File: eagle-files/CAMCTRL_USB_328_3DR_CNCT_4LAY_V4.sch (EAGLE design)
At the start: 71 parts, among them IC2 lm1117, J1 ICSP, Q1 12MHz, U1 M3421E, U2 ATMEGA168, U3 3.3V_REG, U4 TS3USB30EDGSR, Y1 16MHz

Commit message: Updated Code and Board
Updated test code with new object info handling, zooming command and
some extra clean-ups.
Board updated with replaced LED's resistors.
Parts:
- R13, R2, R6: value 1K -> 220R
- R14: value 330 -> 100R
- R17, R18: value 270R -> 220R
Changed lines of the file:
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@@
 <part name="Y1" library="SparkFun-FreqCtrl" deviceset="RESONATOR" device="16MHZ" value="16MHz"/>
 <part name="Q1" library="SparkFun-FreqCtrl" deviceset="CRYSTAL" device="5X3" value="12MHz"/>
-<part name="R2" library="pel_dipol_comp" deviceset="RESISTOR" device="-0402" value="1K"/>
+<part name="R2" library="pel_dipol_comp" deviceset="RESISTOR" device="-0402" value="220R"/>
 <part name="C2" library="pel_dipol_comp" deviceset="CAPACITOR" device="-0402" value="0.1uF"/>
 <part name="P+1" library="supply1" deviceset="VCC" device="" value="5V"/>
@@
 <part name="LED2" library="pel_dipol_comp" deviceset="LED" device="-0603" value="RED"/>
 <part name="GND16" library="SparkFun" deviceset="GND" device=""/>
-<part name="R14" library="pel_dipol_comp" deviceset="RESISTOR" device="-0402" value="330"/>
+<part name="R14" library="pel_dipol_comp" deviceset="RESISTOR" device="-0402" value="100R"/>
 <part name="C10" library="SparkFun" deviceset="CAP_POL" device="1206" value="10uF"/>
 <part name="GND17" library="SparkFun" deviceset="GND" device=""/>
@@
 <part name="R1" library="pel_dipol_comp" deviceset="RESISTOR" device="-0402" value="33 1%"/>
 <part name="R5" library="pel_dipol_comp" deviceset="RESISTOR" device="-0402" value="33 1%"/>
-<part name="R6" library="pel_dipol_comp" deviceset="RESISTOR" device="-0402" value="1K"/>
+<part name="R6" library="pel_dipol_comp" deviceset="RESISTOR" device="-0402" value="220R"/>
 <part name="GND18" library="supply1" deviceset="GND" device=""/>
 <part name="LED3" library="pel_dipol_comp" deviceset="LED" device="-0603" value="BLUE"/>
@@
 <part name="SJ1" library="SparkFun-Passives" deviceset="SOLDERJUMPER_2WAY" device="PASTE2&amp;3"/>
 <part name="SJ2" library="SparkFun-Passives" deviceset="SOLDERJUMPER-OLD" device="NO"/>
-<part name="R13" library="pel_dipol_comp" deviceset="RESISTOR" device="-0402" value="1K"/>
+<part name="R13" library="pel_dipol_comp" deviceset="RESISTOR" device="-0402" value="220R"/>
 <part name="LED4" library="pel_dipol_comp" deviceset="LED" device="-0603" value="BLUE"/>
 <part name="GND23" library="SparkFun-Aesthetics" deviceset="GND" device=""/>
@@
 <part name="C13" library="pel_dipol_comp" deviceset="CAPACITOR" device="-0402" value="0.1uF"/>
 <part name="GND30" library="SparkFun" deviceset="GND" device=""/>
-<part name="R17" library="pel_dipol_comp" deviceset="RESISTOR" device="-0402" value="270R"/>
-<part name="R18" library="pel_dipol_comp" deviceset="RESISTOR" device="-0402" value="270R"/>
+<part name="R17" library="pel_dipol_comp" deviceset="RESISTOR" device="-0402" value="220R"/>
+<part name="R18" library="pel_dipol_comp" deviceset="RESISTOR" device="-0402" value="220R"/>
 <part name="LED5" library="pel_dipol_comp" deviceset="LED" device="-0603" value="GREEN"/>
 <part name="LED6" library="pel_dipol_comp" deviceset="LED" device="-0603" value="RED"/>
@@
 <instance part="GND10" gate="1" x="45.72" y="185.42"/>
 <instance part="U$3" gate="G$1" x="45.72" y="220.98"/>
-<instance part="R4" gate="G$1" x="45.72" y="210.82" rot="R90"/>
+<instance part="R4" gate="G$1" x="45.72" y="210.82" smashed="yes" rot="R90">
+<attribute name="VALUE" x="48.768" y="210.82" size="1.778" layer="96" rot="R90"/>
+<attribute name="NAME" x="48.768" y="205.74" size="1.778" layer="95" rot="R90"/>
+</instance>
 <instance part="C14" gate="G$1" x="38.1" y="205.74" rot="R90"/>
 <instance part="C1" gate="G$1" x="96.52" y="391.16"/>

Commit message: Prototype V2
USB interruption line added;
VCC vs 5V wrong propagation corrected.
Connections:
- removed net D9: DIGITAL_PINS.2, U2.PB1(OC1A)
- removed net N$11: R3.2, U1.INT
- removed net VCC: C6.1, U4.VCC, U5.VCCB
- new net INT: R3.2, U1.INT, U2.PB1(OC1A)
- net 3.3V: now also U4.VCC
- net 5V: now also C6.1, U5.VCCB
- net D2: now also DIGITAL_PINS.2
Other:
- moved on the sheet: C3, C4, C5, C6

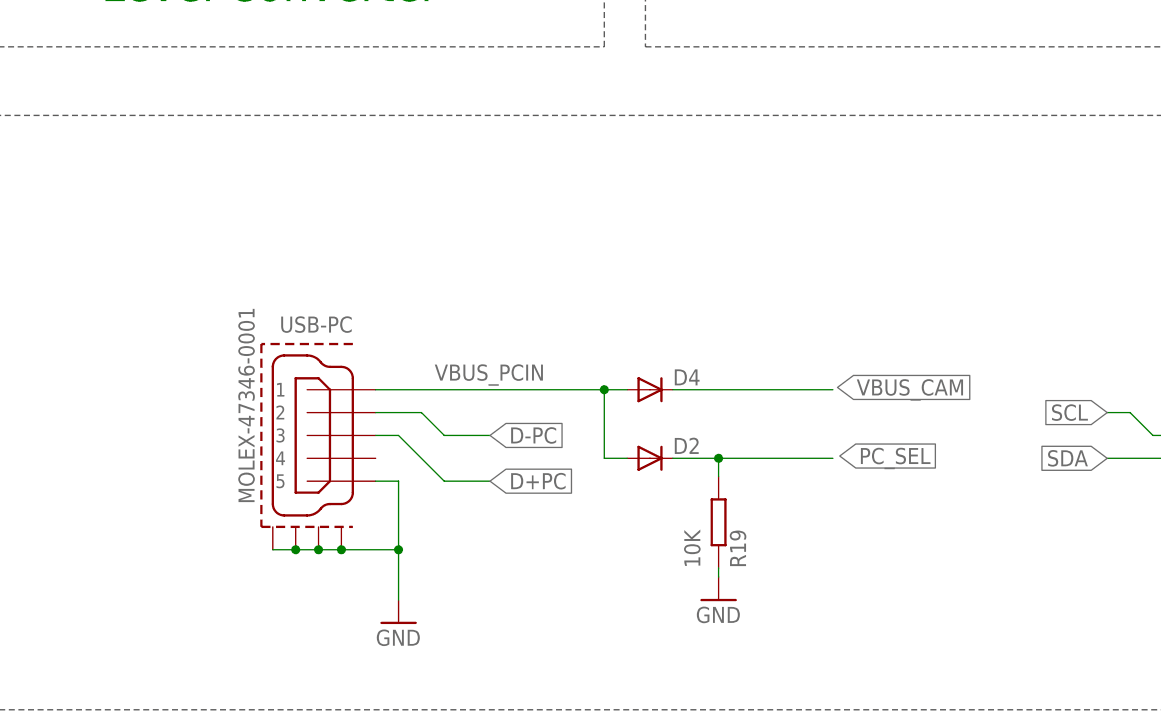
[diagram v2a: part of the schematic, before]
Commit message: Prototype V2.1
4k7 resistor added to the USB-Mux's "select" pin.
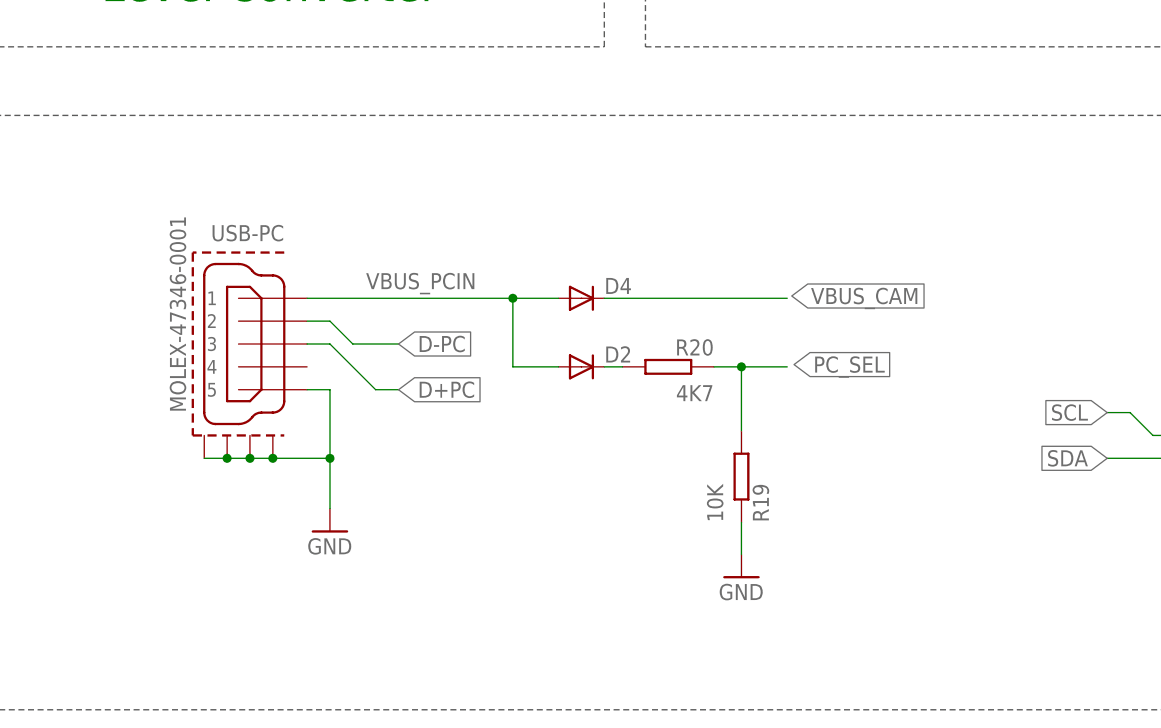
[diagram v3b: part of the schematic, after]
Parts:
- added R20: 4K7, pel_dipol_comp:RESISTOR-0402
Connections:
- new net N$28: D2.C, R20.2
- net PC_SEL: now also R20.1; no longer D2.C
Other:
- moved on the sheet: D2, D4, R19, USB-PC
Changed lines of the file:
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@@
 <part name="U$11" library="SparkFun" deviceset="5V" device=""/>
 <part name="U$13" library="SparkFun" deviceset="5V" device=""/>
+<part name="R20" library="pel_dipol_comp" deviceset="RESISTOR" device="-0402" value="4K7"/>
 </parts>
 <sheets>
@@
 <instance part="P+32" gate="G$1" x="342.9" y="139.7"/>
 <instance part="GND34" gate="1" x="342.9" y="124.46"/>
-<instance part="USB-PC" gate="G$1" x="246.38" y="134.62" rot="MR0"/>
+<instance part="USB-PC" gate="G$1" x="238.76" y="144.78" rot="MR0"/>
 <instance part="U4" gate="A" x="492.76" y="203.2"/>
 <instance part="GND5" gate="1" x="469.9" y="182.88"/>
 <instance part="USB_HOST" gate="G$1" x="294.64" y="269.24" rot="MR0"/>
-<instance part="D4" gate="G$1" x="281.94" y="139.7" smashed="yes">
-<attribute name="NAME" x="284.48" y="140.1826" size="1.778" layer="95"/>
+<instance part="D4" gate="G$1" x="274.32" y="149.86" smashed="yes">
+<attribute name="NAME" x="276.86" y="150.3426" size="1.778" layer="95"/>
 </instance>
-<instance part="R19" gate="G$1" x="289.56" y="124.968" rot="R90"/>
-<instance part="GND32" gate="1" x="289.56" y="116.332"/>
-<instance part="D2" gate="G$1" x="281.94" y="132.08" smashed="yes">
-<attribute name="NAME" x="284.48" y="132.5626" size="1.778" layer="95"/>
+<instance part="R19" gate="G$1" x="292.1" y="130.048" rot="R90"/>
+<instance part="GND32" gate="1" x="292.1" y="118.872"/>
+<instance part="D2" gate="G$1" x="274.32" y="142.24" smashed="yes">
+<attribute name="NAME" x="276.86" y="142.7226" size="1.778" layer="95"/>
 </instance>
 <instance part="FRAME1" gate="G$1" x="0" y="0"/>
 <instance part="FRAME1" gate="G$2" x="452.12" y="0"/>
-<instance part="GND33" gate="1" x="254" y="113.792"/>
+<instance part="GND33" gate="1" x="246.38" y="123.952"/>
 <instance part="I2C" gate="G$1" x="353.06" y="134.62"/>
 <instance part="DIGITAL_PINS" gate="G$1" x="121.92" y="139.7" rot="R180"/>
@@
 <instance part="U$11" gate="G$1" x="149.86" y="292.1"/>
 <instance part="U$13" gate="G$1" x="223.52" y="281.94"/>
+<instance part="R20" gate="G$1" x="283.972" y="142.24" rot="R180"/>
 </instances>
 <busses>
@@
 </segment>
 <segment>
-<wire x1="254" y1="129.54" x2="254" y2="121.92" width="0.1524" layer="91"/>
+<wire x1="246.38" y1="139.7" x2="246.38" y2="132.08" width="0.1524" layer="91"/>
 <pinref part="USB-PC" gate="G$1" pin="5"/>
-<wire x1="254" y1="121.92" x2="254" y2="116.332" width="0.1524" layer="91"/>
-<wire x1="254" y1="129.54" x2="251.46" y2="129.54" width="0.1524" layer="91"/>
+<wire x1="246.38" y1="132.08" x2="246.38" y2="126.492" width="0.1524" layer="91"/>
+<wire x1="246.38" y1="139.7" x2="243.84" y2="139.7" width="0.1524" layer="91"/>
 <pinref part="GND33" gate="1" pin="GND"/>
 <pinref part="USB-PC" gate="G$1" pin="GND1"/>
-<wire x1="247.65" y1="121.92" x2="254" y2="121.92" width="0.1524" layer="91"/>
-<junction x="254" y="121.92"/>
+<wire x1="240.03" y1="132.08" x2="246.38" y2="132.08" width="0.1524" layer="91"/>
+<junction x="246.38" y="132.08"/>
 <pinref part="USB-PC" gate="G$1" pin="GND2"/>
-<wire x1="247.65" y1="121.92" x2="245.11" y2="121.92" width="0.1524" layer="91"/>
-<junction x="247.65" y="121.92"/>
+<wire x1="240.03" y1="132.08" x2="237.49" y2="132.08" width="0.1524" layer="91"/>
+<junction x="240.03" y="132.08"/>
 <pinref part="USB-PC" gate="G$1" pin="GND3"/>
-<wire x1="245.11" y1="121.92" x2="242.57" y2="121.92" width="0.1524" layer="91"/>
-<junction x="245.11" y="121.92"/>
+<wire x1="237.49" y1="132.08" x2="234.95" y2="132.08" width="0.1524" layer="91"/>
+<junction x="237.49" y="132.08"/>
 <pinref part="USB-PC" gate="G$1" pin="GND4"/>
-<wire x1="242.57" y1="121.92" x2="240.03" y2="121.92" width="0.1524" layer="91"/>
-<junction x="242.57" y="121.92"/>
+<wire x1="234.95" y1="132.08" x2="232.41" y2="132.08" width="0.1524" layer="91"/>
+<junction x="234.95" y="132.08"/>
 </segment>
 <segment>
@@
 <pinref part="R19" gate="G$1" pin="1"/>
 <pinref part="GND32" gate="1" pin="GND"/>
-<wire x1="289.56" y1="119.888" x2="289.56" y2="118.872" width="0.1524" layer="91"/>
+<wire x1="292.1" y1="124.968" x2="292.1" y2="121.412" width="0.1524" layer="91"/>
 </segment>
 <segment>
@@
 <net name="VBUS_PCIN" class="0">
 <segment>
-<wire x1="251.46" y1="139.7" x2="276.86" y2="139.7" width="0.1524" layer="91"/>
-<label x="270.256" y="142.494" size="1.778" layer="95" rot="R180"/>
+<wire x1="243.84" y1="149.86" x2="266.7" y2="149.86" width="0.1524" layer="91"/>
+<label x="262.636" y="152.654" size="1.778" layer="95" rot="R180"/>
 <pinref part="USB-PC" gate="G$1" pin="1"/>
 <pinref part="D4" gate="G$1" pin="A"/>
-<wire x1="276.86" y1="139.7" x2="279.4" y2="139.7" width="0.1524" layer="91"/>
-<junction x="276.86" y="139.7"/>
-<wire x1="276.86" y1="139.7" x2="276.86" y2="132.08" width="0.1524" layer="91"/>
+<wire x1="266.7" y1="149.86" x2="271.78" y2="149.86" width="0.1524" layer="91"/>
+<junction x="266.7" y="149.86"/>
+<wire x1="266.7" y1="149.86" x2="266.7" y2="142.24" width="0.1524" layer="91"/>
 <pinref part="D2" gate="G$1" pin="A"/>
-<wire x1="276.86" y1="132.08" x2="279.4" y2="132.08" width="0.1524" layer="91"/>
+<wire x1="266.7" y1="142.24" x2="271.78" y2="142.24" width="0.1524" layer="91"/>
 </segment>
 </net>
@@
 <segment>
 <pinref part="D4" gate="G$1" pin="C"/>
-<wire x1="284.48" y1="139.7" x2="302.26" y2="139.7" width="0.1524" layer="91"/>
-<label x="302.768" y="139.954" size="1.778" layer="95" xref="yes"/>
+<wire x1="276.86" y1="149.86" x2="297.18" y2="149.86" width="0.1524" layer="91"/>
+<label x="297.688" y="150.114" size="1.778" layer="95" xref="yes"/>
 </segment>
 </net>
 <net name="D-PC" class="0">
 <segment>
-<wire x1="251.46" y1="137.16" x2="256.54" y2="137.16" width="0.1524" layer="91"/>
-<wire x1="256.54" y1="137.16" x2="259.08" y2="134.62" width="0.1524" layer="91"/>
-<wire x1="259.08" y1="134.62" x2="264.16" y2="134.62" width="0.1524" layer="91"/>
-<label x="264.16" y="134.62" size="1.778" layer="95" xref="yes"/>
+<wire x1="243.84" y1="147.32" x2="246.38" y2="147.32" width="0.1524" layer="91"/>
+<wire x1="246.38" y1="147.32" x2="248.92" y2="144.78" width="0.1524" layer="91"/>
+<wire x1="248.92" y1="144.78" x2="254" y2="144.78" width="0.1524" layer="91"/>
+<label x="254" y="144.78" size="1.778" layer="95" xref="yes"/>
 <pinref part="USB-PC" gate="G$1" pin="2"/>
 </segment>
@@
 <net name="D+PC" class="0">
 <segment>
-<wire x1="251.46" y1="134.62" x2="254" y2="134.62" width="0.1524" layer="91"/>
-<wire x1="254" y1="134.62" x2="259.08" y2="129.54" width="0.1524" layer="91"/>
-<wire x1="259.08" y1="129.54" x2="264.16" y2="129.54" width="0.1524" layer="91"/>
-<label x="264.16" y="129.54" size="1.778" layer="95" xref="yes"/>
+<wire x1="243.84" y1="144.78" x2="246.38" y2="144.78" width="0.1524" layer="91"/>
+<wire x1="246.38" y1="144.78" x2="251.46" y2="139.7" width="0.1524" layer="91"/>
+<wire x1="251.46" y1="139.7" x2="254" y2="139.7" width="0.1524" layer="91"/>
+<label x="254" y="139.7" size="1.778" layer="95" xref="yes"/>
 <pinref part="USB-PC" gate="G$1" pin="3"/>
 </segment>
@@
 </segment>
 <segment>
+<label x="297.942" y="142.494" size="1.778" layer="95" xref="yes"/>
+<wire x1="292.1" y1="135.128" x2="292.1" y2="142.24" width="0.1524" layer="91"/>
+<pinref part="R19" gate="G$1" pin="2"/>
+<pinref part="R20" gate="G$1" pin="1"/>
+<wire x1="289.052" y1="142.24" x2="292.1" y2="142.24" width="0.1524" layer="91"/>
+<wire x1="292.1" y1="142.24" x2="297.18" y2="142.24" width="0.1524" layer="91"/>
+<junction x="292.1" y="142.24"/>
+</segment>
+</net>
+<net name="N$28" class="0">
+<segment>
 <pinref part="D2" gate="G$1" pin="C"/>
-<wire x1="284.48" y1="132.08" x2="289.56" y2="132.08" width="0.1524" layer="91"/>
-<label x="303.022" y="132.334" size="1.778" layer="95" xref="yes"/>
-<wire x1="289.56" y1="132.08" x2="302.26" y2="132.08" width="0.1524" layer="91"/>
-<wire x1="289.56" y1="130.048" x2="289.56" y2="132.08" width="0.1524" layer="91"/>
-<junction x="289.56" y="132.08"/>
-<pinref part="R19" gate="G$1" pin="2"/>
-</segment>
-</net>
+<pinref part="R20" gate="G$1" pin="2"/>
+<wire x1="276.86" y1="142.24" x2="278.892" y2="142.24" width="0.1524" layer="91"/>
+</segment>
+</net>

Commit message: Level Converter Replacement
TXB0104PWR replaced by a TXS0104PWR (larger current draw on the IO). A
10K OE resistor was added as well.
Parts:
- added R21: 10K, pel_dipol_comp:RESISTOR-0402
- U5: device adafruit:TXB0104PWR -> adafruit:TXS0104PWR
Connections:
- new net N$29: R21.2, U5.OE
- net 3.3V: now also R21.1
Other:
- moved on the sheet: C5
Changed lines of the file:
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@@
 <part name="U$4" library="SparkFun" deviceset="5V" device=""/>
 <part name="OK2" library="optocoupler" deviceset="ILD2*" device="" technology="05"/>
-<part name="U5" library="adafruit" deviceset="TXB0104PWR" device=""/>
+<part name="U5" library="adafruit" deviceset="TXS0104PWR" device=""/>
 <part name="P+3" library="SparkFun" deviceset="3.3V" device=""/>
 <part name="C5" library="pel_dipol_comp" deviceset="CAPACITOR" device="-0402" value="0.1uF"/>
@@
 <part name="U$13" library="SparkFun" deviceset="5V" device=""/>
 <part name="R20" library="pel_dipol_comp" deviceset="RESISTOR" device="-0402" value="4K7"/>
+<part name="R21" library="pel_dipol_comp" deviceset="RESISTOR" device="-0402" value="10K"/>
 </parts>
 <sheets>
@@
 <instance part="U5" gate="G$1" x="226.06" y="248.92" rot="MR0"/>
 <instance part="P+3" gate="G$1" x="228.6" y="281.94"/>
-<instance part="C5" gate="G$1" x="243.84" y="274.32" rot="R90"/>
+<instance part="C5" gate="G$1" x="248.92" y="274.32" rot="R90"/>
 <instance part="C6" gate="G$1" x="205.74" y="274.32" rot="R270"/>
 <instance part="GND13" gate="1" x="226.06" y="231.14"/>
 <instance part="GND24" gate="1" x="193.04" y="271.78"/>
-<instance part="GND25" gate="1" x="256.54" y="271.78"/>
+<instance part="GND25" gate="1" x="264.16" y="271.78"/>
 <instance part="USB1" gate="G$1" x="454.66" y="393.7" rot="MR0"/>
 <instance part="GND9" gate="1" x="462.28" y="373.38"/>
@@
 <instance part="U$13" gate="G$1" x="223.52" y="281.94"/>
 <instance part="R20" gate="G$1" x="283.972" y="142.24" rot="R180"/>
+<instance part="R21" gate="G$1" x="243.84" y="261.62" rot="R270"/>
 </instances>
 <busses>
@@
 <pinref part="C5" gate="G$1" pin="2"/>
 <pinref part="GND25" gate="1" pin="GND"/>
-<wire x1="248.92" y1="274.32" x2="256.54" y2="274.32" width="0.1524" layer="91"/>
+<wire x1="254" y1="274.32" x2="264.16" y2="274.32" width="0.1524" layer="91"/>
 </segment>
 <segment>
@@
 <pinref part="C5" gate="G$1" pin="1"/>
 <wire x1="228.6" y1="274.32" x2="228.6" y2="266.7" width="0.1524" layer="91"/>
-<wire x1="228.6" y1="274.32" x2="241.3" y2="274.32" width="0.1524" layer="91"/>
+<wire x1="228.6" y1="274.32" x2="243.84" y2="274.32" width="0.1524" layer="91"/>
 <junction x="228.6" y="274.32"/>
+<pinref part="R21" gate="G$1" pin="1"/>
+<wire x1="243.84" y1="274.32" x2="246.38" y2="274.32" width="0.1524" layer="91"/>
+<wire x1="243.84" y1="266.7" x2="243.84" y2="274.32" width="0.1524" layer="91"/>
+<junction x="243.84" y="274.32"/>
 </segment>
 </net>
@@
 </segment>
 </net>
+<net name="N$29" class="0">
+<segment>
+<pinref part="U5" gate="G$1" pin="OE"/>
+<pinref part="R21" gate="G$1" pin="2"/>
+<wire x1="241.3" y1="256.54" x2="243.84" y2="256.54" width="0.1524" layer="91"/>
+</segment>
+</net>
